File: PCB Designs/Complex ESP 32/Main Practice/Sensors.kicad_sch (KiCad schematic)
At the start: 21 parts, among them Q1 TEMT6000X01, U2 BME280, U7 MAX4466EXK, U9 ISM330DLCTR

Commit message: Saved UI
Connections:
- net GND: no longer U9.1 (SDO/SAO)
- no-connect marks 5 -> 6
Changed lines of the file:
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@@
 		(color 0 0 0 0)
 	)
-	(junction
-		(at 90.17 90.17)
-		(diameter 0)
-		(color 0 0 0 0)
-	)
 	(no_connect
 		(at 80.01 97.79)
@@
 		(at 80.01 87.63)
 	)
+	(no_connect
+		(at 80.01 90.17)
+	)
 	(wire
 		(pts
@@
 	(wire
 		(pts
-			(xy 90.17 88.9) (xy 90.17 90.17)
+			(xy 90.17 88.9) (xy 90.17 102.87)
 		)
 		(stroke
@@
 	(wire
 		(pts
-			(xy 80.01 90.17) (xy 90.17 90.17)
-		)
-		(stroke
-			(width 0)
-			(type default)
-		)
-	)
-	(wire
-		(pts
 			(xy 215.265 60.325) (xy 219.075 60.325)
 		)
@@
 		)
 		(stroke
-			(width 0)
-			(type default)
-		)
-	)
-	(wire
-		(pts
-			(xy 90.17 90.17) (xy 90.17 102.87)
-		)
-		(stroke

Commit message: Started Schematics of footprint
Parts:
- MK1: footprint CMC-5042PF-AC:CUI_CMC-5042PF-AC -> Footprints:CUI_CMC-5042PF-AC
- Q1: footprint TEMT6000X01:TRANS_TEMT6000X01 -> Footprints:TRANS_TEMT6000X01
- U2: footprint BME280:PSON65P250X250X100-8N -> Footprints:PSON65P250X250X100-8N
- U7: footprint MAX4466EXK:SOT65P210X110-5N -> Footprints:SOT65P210X110-5N
- U9: footprint ISM330DLCTR:PQFN50P250X300X86-14N -> Footprints:QFN50P400X400X100-21N
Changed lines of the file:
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@@
 			)
 		)
-		(property "Footprint" "ISM330DLCTR:PQFN50P250X300X86-14N"
+		(property "Footprint" "Footprints:QFN50P400X400X100-21N"
 			(at 62.23 90.17 0)
 			(hide yes)
@@
 			)
 		)
-		(property "Footprint" "CMC-5042PF-AC:CUI_CMC-5042PF-AC"
+		(property "Footprint" "Footprints:CUI_CMC-5042PF-AC"
 			(at 138.43 45.72 0)
 			(hide yes)
@@
 			)
 		)
-		(property "Footprint" "TEMT6000X01:TRANS_TEMT6000X01"
+		(property "Footprint" "Footprints:TRANS_TEMT6000X01"
 			(at 104.14 33.02 0)
 			(hide yes)
@@
 			)
 		)
-		(property "Footprint" "BME280:PSON65P250X250X100-8N"
+		(property "Footprint" "Footprints:PSON65P250X250X100-8N"
 			(at 62.23 39.37 0)
 			(hide yes)
@@
 			)
 		)
-		(property "Footprint" "MAX4466EXK:SOT65P210X110-5N"
+		(property "Footprint" "Footprints:SOT65P210X110-5N"
 			(at 198.755 45.72 0)
 			(hide yes)

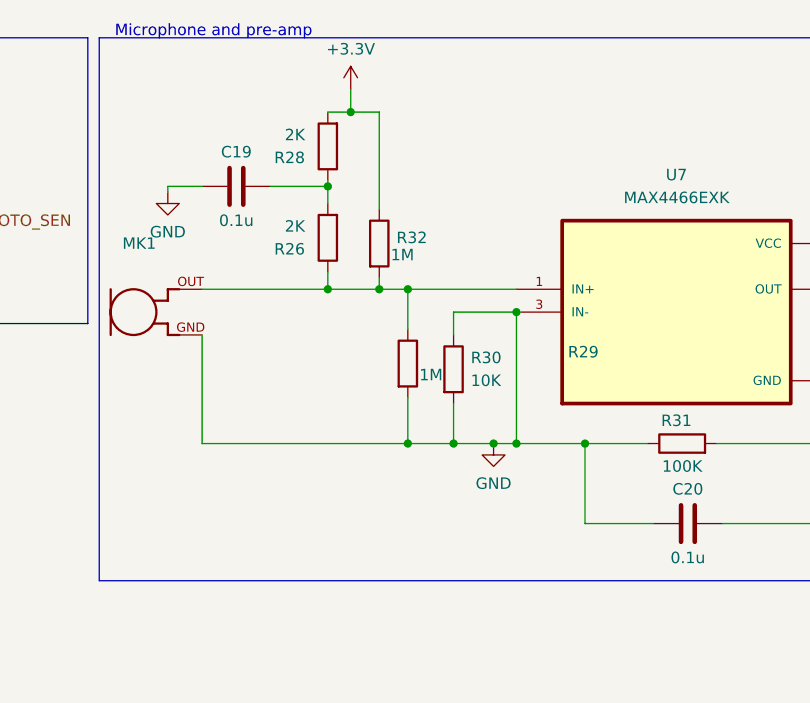
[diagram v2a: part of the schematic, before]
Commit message: reordered components around for optimal wiring
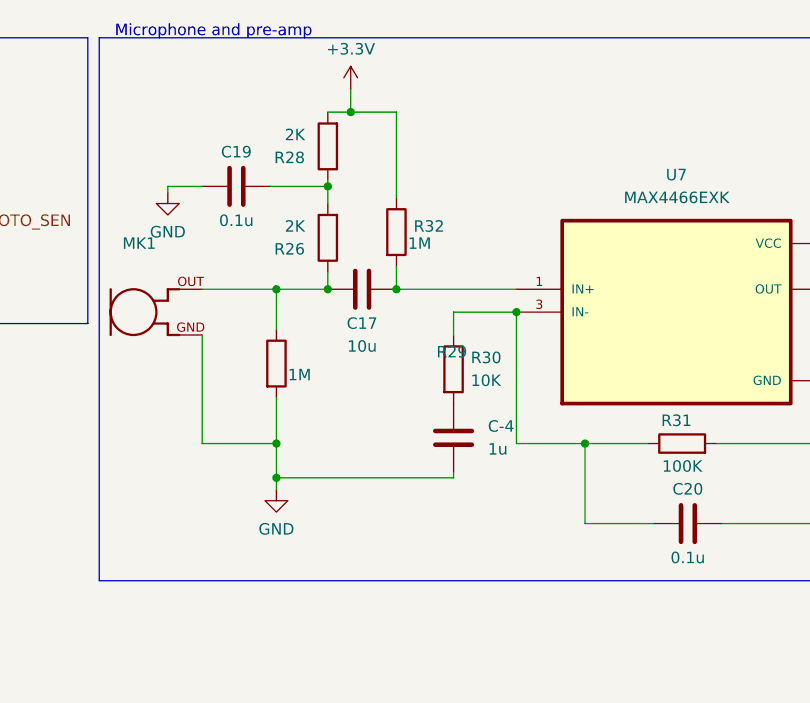
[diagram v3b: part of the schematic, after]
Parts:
- added C-4: 1u, Capacitor_SMD:C_0805_2012Metric, symbol Device:C
- added C17: 10u, Capacitor_SMD:C_0805_2012Metric, symbol Device:C
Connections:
- net GND: now also C-4.2; no longer C20.1, R30.1, R30.2, R31.1, U7.3 (IN-)
- net at MK1.OUT, R26.1, R29.1: now also C17.1; no longer R32.2, U7.1 (IN+)
- new net: C20.1, R30.1, R31.1, U7.3 (IN-)
- new net: C-4.1, R30.2
- new net: C17.2, R32.2, U7.1 (IN+)
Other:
- moved on the sheet: R29, R32
